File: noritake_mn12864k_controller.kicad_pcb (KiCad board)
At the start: 4 copper layers, 85 x 45.5 mm, 148 parts, among them J1 Conn_01x11, J2 USB_C_Receptacle_USB2.0, J3 TagConnect_TC2030_SWD, J4 Conn_01x18, Q1 AO3400A, Q10 2N7002, Q11 LBSS84LT1G, Q12 2N7002, Q13 TO-252, Q14 CJT04N15, Q15 2N7002, Q16 LBSS84LT1G, Q17 2N7002, Q18 S9015, Q2 AO3400A, Q3 S9015, Q4 AO3401A, Q5 AO3401A, Q6 S9015, Q7 2N7002, Q8 LBSS84LT1G, Q9 2N7002, T1 Wuerth 760390013, T2 Wuerth 760390013, T3 Wuerth 760390013, U1 SN74AVC8T245PW, U10 SRV05-4, U11 SRV05-4, U12 SRV05-4, U2 74HC14, U3 CD4051B, U4 MN12864K, U5 STM32F730R8T6, U6 NE555D, U7 74HC08, U8 SRV05-4, U9 XC6206PxxxMR

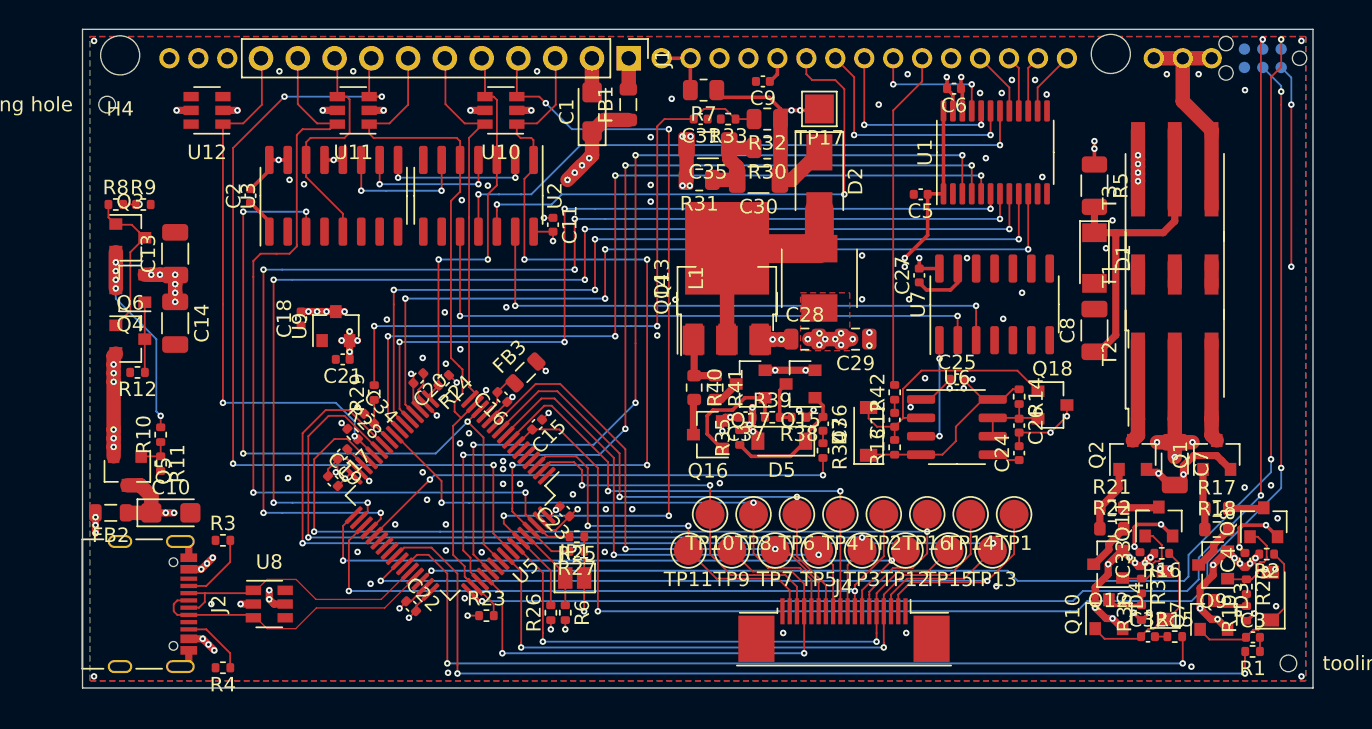
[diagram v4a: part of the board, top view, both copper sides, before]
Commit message: Add silkscreen markings
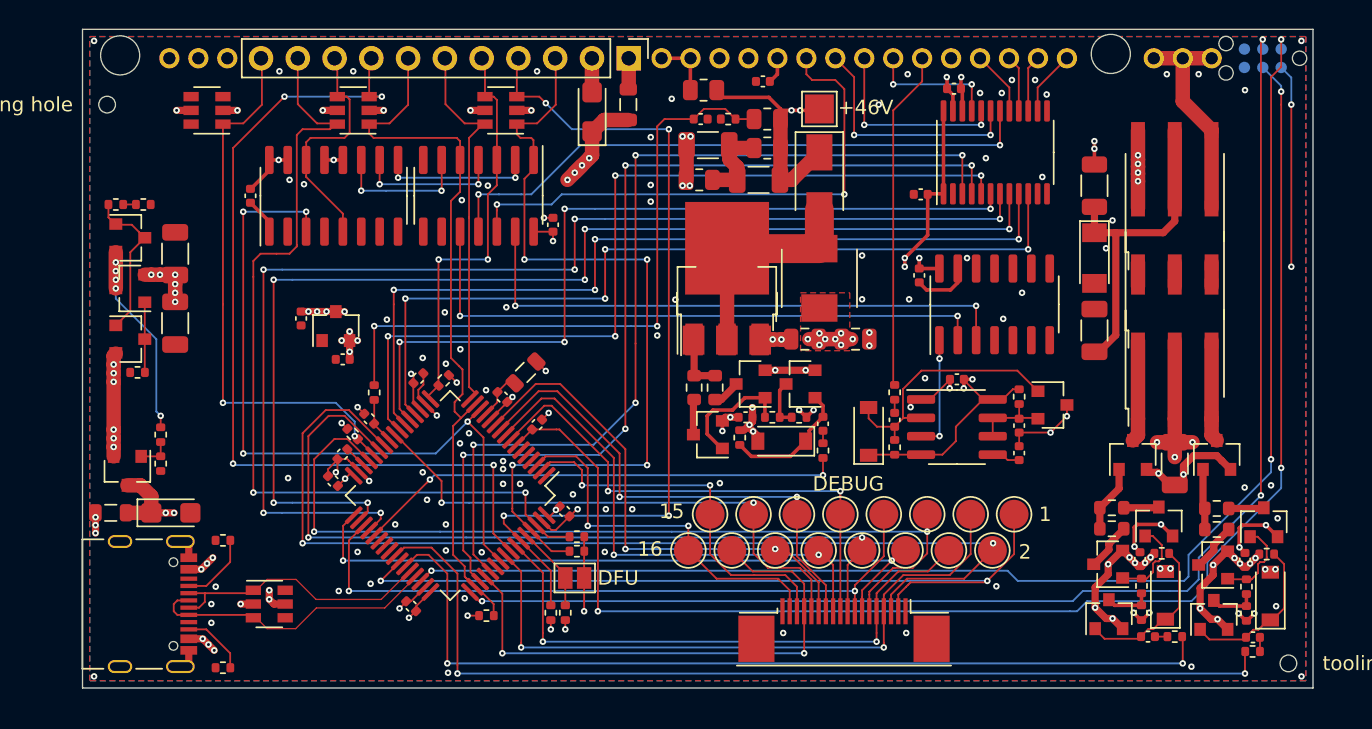
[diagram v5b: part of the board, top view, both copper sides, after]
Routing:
- net GND: vias 128 -> 131
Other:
- board text added: "+46V"
- board text added: "1"
- board text added: "15"
- board text added: "16"
- board text added: "2"
- board text added: "DEBUG"
- board text added: "DFU"

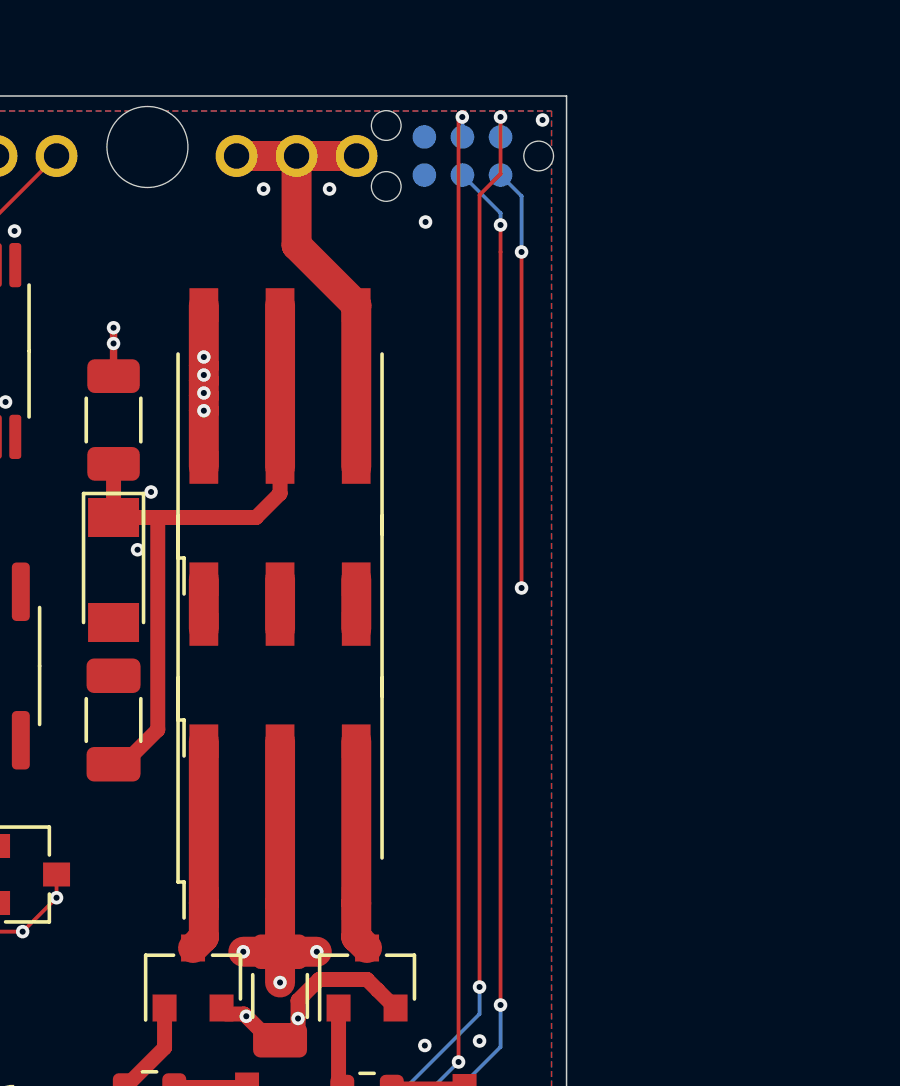
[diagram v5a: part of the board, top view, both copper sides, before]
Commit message: Add more silkscreen markings
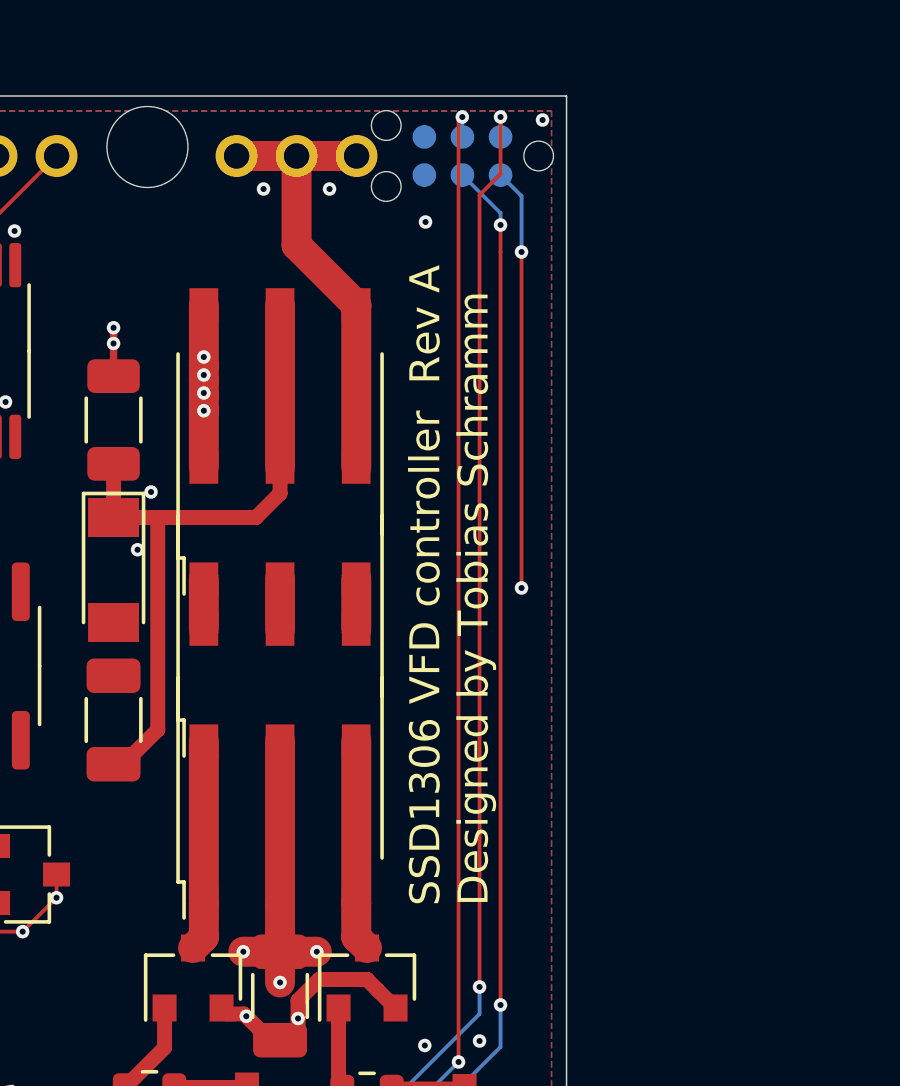
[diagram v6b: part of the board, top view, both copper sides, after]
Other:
- board text added: "SSD1306 VFD controller Rev A Designed by Tobias Schramm"
- board text added: "SWD"
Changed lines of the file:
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@@
   (general
     (thickness 1.6)
-    (drawings 12)
+    (drawings 14)
     (tracks 1486)
     (zones 0)
@@
     )
   )
+  (gr_text SWD (at 181.8 101.1) (layer B.SilkS)
+    (effects (font (size 1 1) (thickness 0.15)) (justify mirror))
+  )
+  (gr_text "SSD1306 VFD controller  Rev A\nDesigned by Tobias Schramm" (at 181.1 123.5 90) (layer F.SilkS)
+    (effects (font (size 1 1) (thickness 0.15)) (justify left))
+  )
   (gr_text +46V (at 154.1 101.9) (layer F.SilkS)

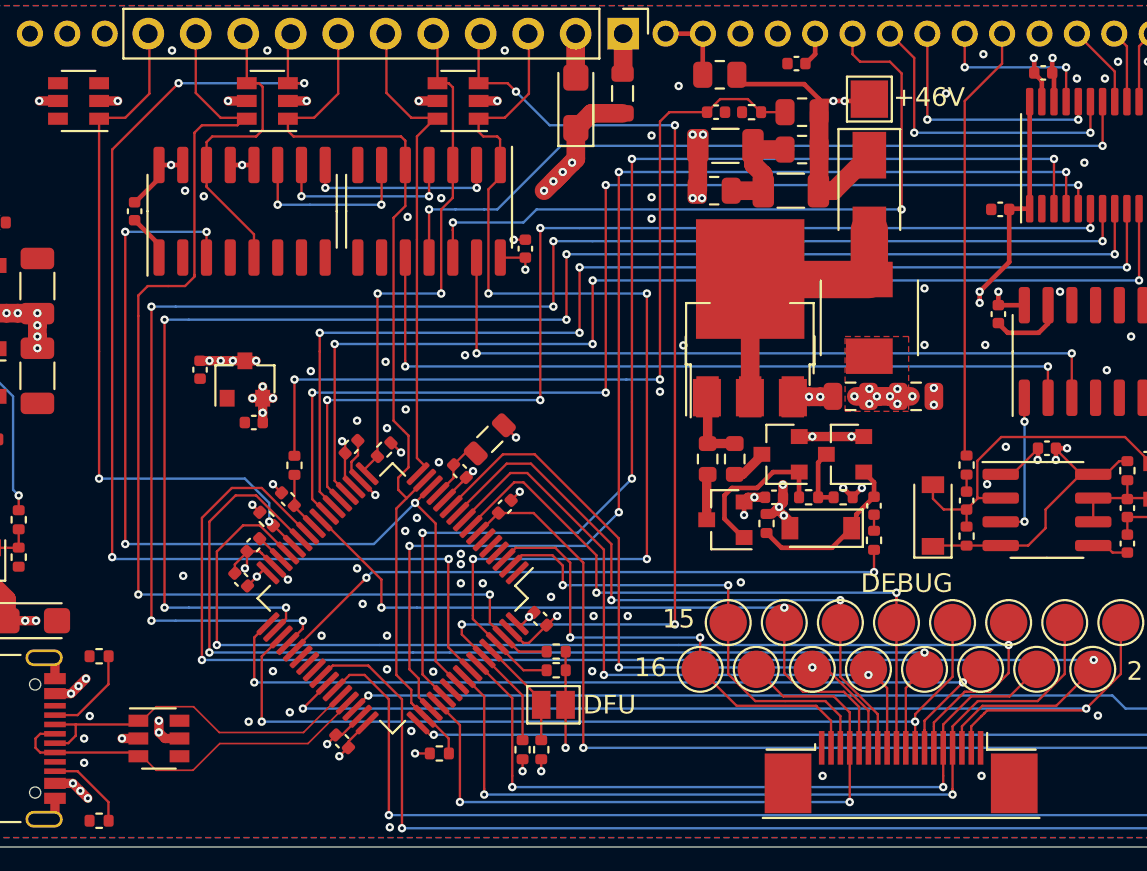
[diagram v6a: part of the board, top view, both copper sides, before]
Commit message: Add pin 1 indicators
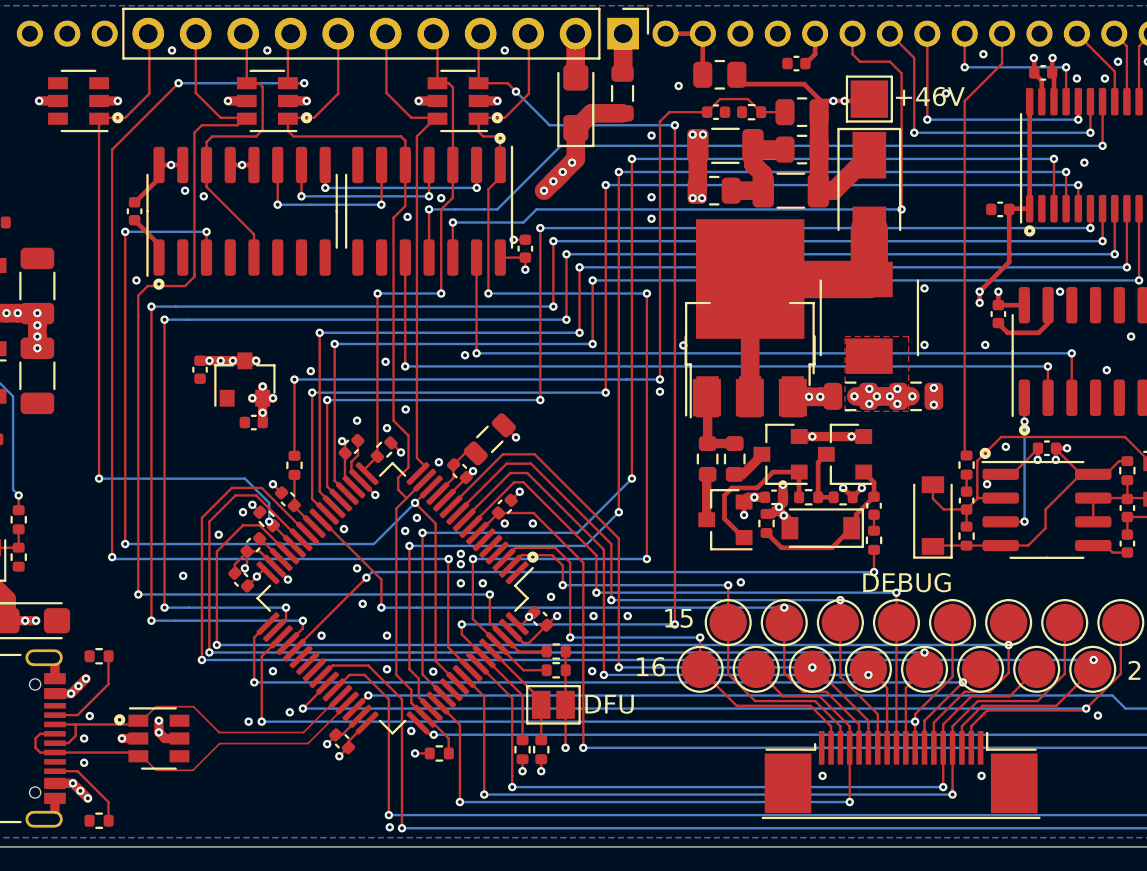
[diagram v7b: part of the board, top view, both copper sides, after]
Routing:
- net /DBG12: track 38.7 -> 38.1 mm
- net GND: vias 131 -> 137
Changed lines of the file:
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@@
   (general
     (thickness 1.6)
-    (drawings 14)
-    (tracks 1486)
+    (drawings 24)
+    (tracks 1494)
     (zones 0)
     (modules 148)
@@
   )
   (setup
-    (last_trace_width 0.09)
+    (last_trace_width 0.127)
     (user_trace_width 0.127)
     (user_trace_width 0.25)
@@
     )
   )
+  (gr_circle (center 159.475 109.05) (end 159.575 109.05) (layer F.SilkS) (width 0.4))
+  (gr_circle (center 159.2 119.7) (end 159.3 119.7) (layer F.SilkS) (width 0.4))
+  (gr_circle (center 157.1 120.95) (end 157.2 120.95) (layer F.SilkS) (width 0.4))
+  (gr_circle (center 112.9 111.9) (end 113 111.9) (layer F.SilkS) (width 0.4))
+  (gr_circle (center 131.15 104.1) (end 131.25 104.1) (layer F.SilkS) (width 0.4))
+  (gr_circle (center 131 103) (end 131.1 103) (layer F.SilkS) (width 0.4))
+  (gr_circle (center 120.8 103) (end 120.9 103) (layer F.SilkS) (width 0.4))
+  (gr_circle (center 110.7 103) (end 110.8 103) (layer F.SilkS) (width 0.4))
+  (gr_circle (center 110.8 135.2) (end 110.9 135.2) (layer F.SilkS) (width 0.4))
+  (gr_circle (center 132.9 126.5) (end 133 126.5) (layer F.SilkS) (width 0.4))
   (gr_text SWD (at 181.8 101.1) (layer B.SilkS)
     (effects (font (size 1 1) (thickness 0.15)) (justify mirror))
@@
   (via (at 109.2 135) (size 0.45) (drill 0.2) (layers F.Cu B.Cu) (net 5))
   (via (at 108.9 137.5) (size 0.45) (drill 0.2) (layers F.Cu B.Cu) (net 5))
+  (via (at 131.4 124.7) (size 0.45) (drill 0.2) (layers F.Cu B.Cu) (net 5))
+  (via (at 132.9 124.7) (size 0.45) (drill 0.2) (layers F.Cu B.Cu) (net 5))
+  (via (at 116.1 125.3) (size 0.45) (drill 0.2) (layers F.Cu B.Cu) (net 5))
+  (via (at 117.4 124.1) (size 0.45) (drill 0.2) (layers F.Cu B.Cu) (net 5))
+  (via (at 122.8 125) (size 0.45) (drill 0.2) (layers F.Cu B.Cu) (net 5))
+  (via (at 111.7 111.7) (size 0.45) (drill 0.2) (layers F.Cu B.Cu) (net 5))
   (via (at 153.2 117.9) (size 0.45) (drill 0.2) (layers F.Cu B.Cu) (net 6))
   (via (at 152.4 118.3) (size 0.45) (drill 0.2) (layers F.Cu B.Cu) (net 6))
@@
   (segment (start 137.1 128.8) (end 149.35 128.8) (width 0.127) (layer B.Cu) (net 102))
   (segment (start 149.35 128.8) (end 149.35 130) (width 0.127) (layer F.Cu) (net 102))
-  (segment (start 150.85 137.25) (end 150.85 134.706898) (width 0.127) (layer F.Cu) (net 103))
-  (segment (start 150.85 134.706898) (end 148.643102 132.5) (width 0.127) (layer F.Cu) (net 103))
   (segment (start 148.643102 132.5) (end 147.85 132.5) (width 0.127) (layer F.Cu) (net 103))
   (segment (start 128.528948 123.803286) (end 128.528948 123.771052) (width 0.127) (layer F.Cu) (net 103))
@@
   (via (at 147.85 132.4) (size 0.45) (drill 0.2) (layers F.Cu B.Cu) (net 103))
   (segment (start 137.5 132.4) (end 147.85 132.4) (width 0.127) (layer B.Cu) (net 103))
-  (segment (start 150.35 137.25) (end 150.35 134.513796) (width 0.127) (layer F.Cu) (net 104))
-  (segment (start 150.35 134.513796) (end 149.593102 133.756898) (width 0.127) (layer F.Cu) (net 104))
-  (segment (start 149.593102 133.756898) (end 149.536204 133.7) (width 0.127) (layer F.Cu) (net 104))
-  (segment (start 149.536204 133.7) (end 147.35 133.7) (width 0.127) (layer F.Cu) (net 104))
-  (segment (start 147.35 133.7) (end 146.35 132.7) (width 0.127) (layer F.Cu) (net 104))
-  (segment (start 146.35 132.7) (end 146.35 130) (width 0.127) (layer F.Cu) (net 104))
+  (segment (start 150.85 135.65) (end 150.85 135.4) (width 0.127) (layer F.Cu) (net 103))
+  (segment (start 150.85 137.25) (end 150.85 135.65) (width 0.127) (layer F.Cu) (net 103))
+  (segment (start 150.85 135.4) (end 150.85 135.25) (width 0.127) (layer F.Cu) (net 103))
+  (segment (start 150.85 135.25) (end 148.1 132.5) (width 0.127) (layer F.Cu) (net 103))
   (segment (start 121.563946 124.510392) (end 121.610392 124.510392) (width 0.127) (layer F.Cu) (net 104))
   (via (at 146.35 129.2) (size 0.45) (drill 0.2) (layers F.Cu B.Cu) (net 104))
@@
   (segment (start 124.8 129.2) (end 124.8 127.7) (width 0.127) (layer F.Cu) (net 104))
   (segment (start 124.8 127.7) (end 121.55 124.45) (width 0.127) (layer F.Cu) (net 104))
-  (segment (start 149.85 137.25) (end 149.85 134.8) (width 0.127) (layer F.Cu) (net 105))
-  (segment (start 149.85 134.8) (end 149 133.95) (width 0.127) (layer F.Cu) (net 105))
-  (segment (start 149 133.95) (end 146.3 133.95) (width 0.127) (layer F.Cu) (net 105))
+  (segment (start 150.35 137.25) (end 150.35 135.55) (width 0.127) (layer F.Cu) (net 104))
+  (segment (start 150.35 135.55) (end 150.35 135.45) (width 0.127) (layer F.Cu) (net 104))
+  (segment (start 146.35 132.7) (end 146.35 130) (width 0.127) (layer F.Cu) (net 104))
+  (segment (start 148.6 133.7) (end 147.35 133.7) (width 0.127) (layer F.Cu) (net 104))
+  (segment (start 147.35 133.7) (end 146.35 132.7) (width 0.127) (layer F.Cu) (net 104))
+  (segment (start 150.35 135.45) (end 148.6 133.7) (width 0.127) (layer F.Cu) (net 104))
   (segment (start 146.3 133.95) (end 144.85 132.5) (width 0.127) (layer F.Cu) (net 105))
   (via (at 129 139.6) (size 0.45) (drill 0.2) (layers F.Cu B.Cu) (net 105))
@@
   (segment (start 129 139.6) (end 149.85 139.6) (width 0.127) (layer B.Cu) (net 105))
   (segment (start 149.85 136.7) (end 149.85 139.6) (width 0.127) (layer F.Cu) (net 105))
-  (segment (start 149.35 137.25) (end 149.35 135) (width 0.127) (layer F.Cu) (net 106))
-  (segment (start 149.35 135) (end 148.55 134.2) (width 0.127) (layer F.Cu) (net 106))
-  (segment (start 148.55 134.2) (end 146.4 134.2) (width 0.127) (layer F.Cu) (net 106))
+  (segment (start 149.85 137.25) (end 149.85 135.65) (width 0.127) (layer F.Cu) (net 105))
+  (segment (start 148.25 133.95) (end 149.85 135.55) (width 0.127) (layer F.Cu) (net 105))
+  (segment (start 149.85 135.65) (end 149.85 135.55) (width 0.127) (layer F.Cu) (net 105))
+  (segment (start 148.25 133.95) (end 146.3 133.95) (width 0.127) (layer F.Cu) (net 105))
   (segment (start 146.4 134.2) (end 144.8 134.2) (width 0.127) (layer F.Cu) (net 106))
   (segment (start 144.8 134.2) (end 143.35 132.75) (width 0.127) (layer F.Cu) (net 106))
@@
   (segment (start 134.5 126.95) (end 134.5 128) (width 0.127) (layer F.Cu) (net 106))
   (segment (start 133.95 126.4) (end 134.5 126.95) (width 0.127) (layer F.Cu) (net 106))
-  (segment (start 148.85 136.7) (end 148.85 135.25) (width 0.127) (layer F.Cu) (net 107))
-  (segment (start 148.85 135.25) (end 148.0875 134.4875) (width 0.127) (layer F.Cu) (net 107))
-  (segment (start 148.05 134.45) (end 148.0875 134.4875) (width 0.127) (layer F.Cu) (net 107))
-  (segment (start 143.8 134.45) (end 148.05 134.45) (width 0.127) (layer F.Cu) (net 107))
+  (segment (start 149.35 137.25) (end 149.35 135.55) (width 0.127) (layer F.Cu) (net 106))
+  (segment (start 149.35 135.55) (end 148 134.2) (width 0.127) (layer F.Cu) (net 106))
+  (segment (start 148 134.2) (end 146.4 134.2) (width 0.127) (layer F.Cu) (net 106))
   (segment (start 141.85 132.5) (end 143.8 134.45) (width 0.127) (layer F.Cu) (net 107))
   (via (at 141.85 130.8) (size 0.45) (drill 0.2) (layers F.Cu B.Cu) (net 107))
@@
   (segment (start 141.85 130.8) (end 141.85 132.5) (width 0.127) (layer F.Cu) (net 107))
   (segment (start 134.9 130.8) (end 134.9 126.8) (width 0.127) (layer F.Cu) (net 107))
+  (segment (start 143.8 134.45) (end 147.75 134.45) (width 0.127) (layer F.Cu) (net 107))
+  (segment (start 148.85 136.7) (end 148.85 135.55) (width 0.127) (layer F.Cu) (net 107))
+  (segment (start 148.85 135.55) (end 147.75 134.45) (width 0.127) (layer F.Cu) (net 107))
   (segment (start 156.056898 132.5) (end 156.85 132.5) (width 0.127) (layer F.Cu) (net 108))
   (segment (start 153.85 135.75) (end 153.85 135.25) (width 0.127) (layer F.Cu) (net 108))
